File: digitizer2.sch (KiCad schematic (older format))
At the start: 4 parts, among them U1 XC7A35T, U2 FT2232H, U3 MT41J128M16, U4 ADS5403

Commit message: Serial interfaces, cleanup
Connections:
- net ADC_RESET is gone; now on net ADC_SRESET: U4.B12 (SRESET)
- net ADC_SCLK: now also U1.P1 (IO_L4N_T0_34)
- net ADC_SDENB: now also U1.R1 (IO_L7N_T1_34)
- net ADC_SDIO: now also U1.N1 (IO_L4P_T0_34)
- net ADC_SRESET: now reaches U1.N2 (IO_L3N_T0_DQS_34)
- net ADC_SDO: no longer names the net of U4.A10 (SDO)
- no-connect marks 19 -> 20
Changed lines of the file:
@@
 Text Label 13350 9550 0    60   ~ 0
 ADC_SDIO
-Text Label 13350 9650 0    60   ~ 0
-ADC_SDO
 Text Label 13350 9750 0    60   ~ 0
 ADC_SDENB
@@
 USB_CLKOUT
 Text Label 13350 9250 0    60   ~ 0
-ADC_RESET
+ADC_SRESET
+NoConn ~ 13350 9650
+Text Label 9250 1600 0    60   ~ 0
+ADC_SDIO
+Text Label 9250 1500 0    60   ~ 0
+ADC_SRESET
+Text Label 9250 1700 0    60   ~ 0
+ADC_SCLK
+Text Label 9250 2300 0    60   ~ 0
+ADC_SDENB
 $EndSCHEMATC

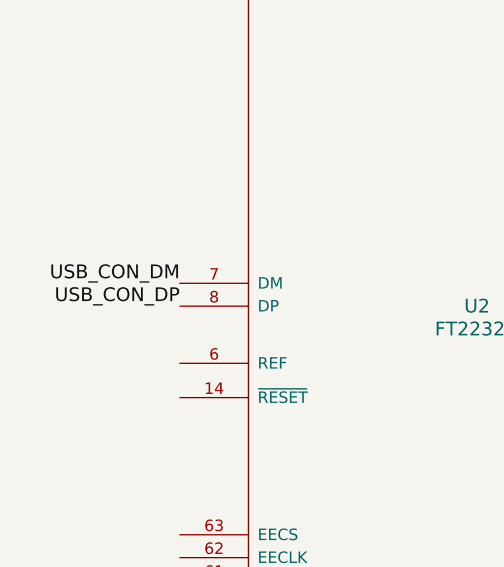
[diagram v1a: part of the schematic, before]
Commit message: Add ADC evaluation board documents, add usb tracks
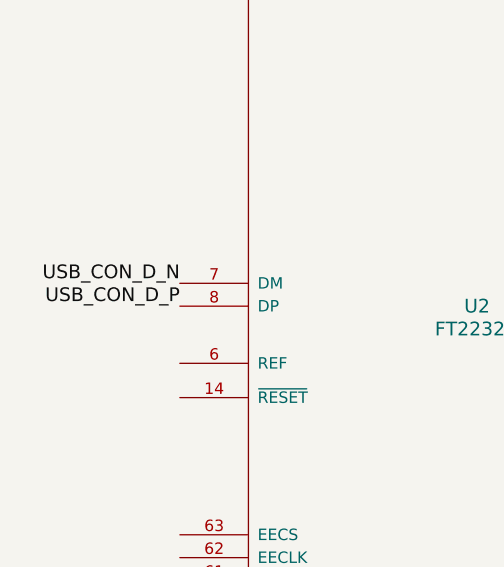
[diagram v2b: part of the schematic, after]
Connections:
- net USB_CON_DM renamed USB_CON_D_N
- net USB_CON_DP renamed USB_CON_D_P
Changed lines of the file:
@@
 Connection ~ 1650 13250
 Text Label 750  10900 2    60   ~ 0
-USB_CON_DM
+USB_CON_D_N
 Text Label 750  11000 2    60   ~ 0
-USB_CON_DP
+USB_CON_D_P
 Text Label 9650 10250 2    60   ~ 0
 ADC_INA_P

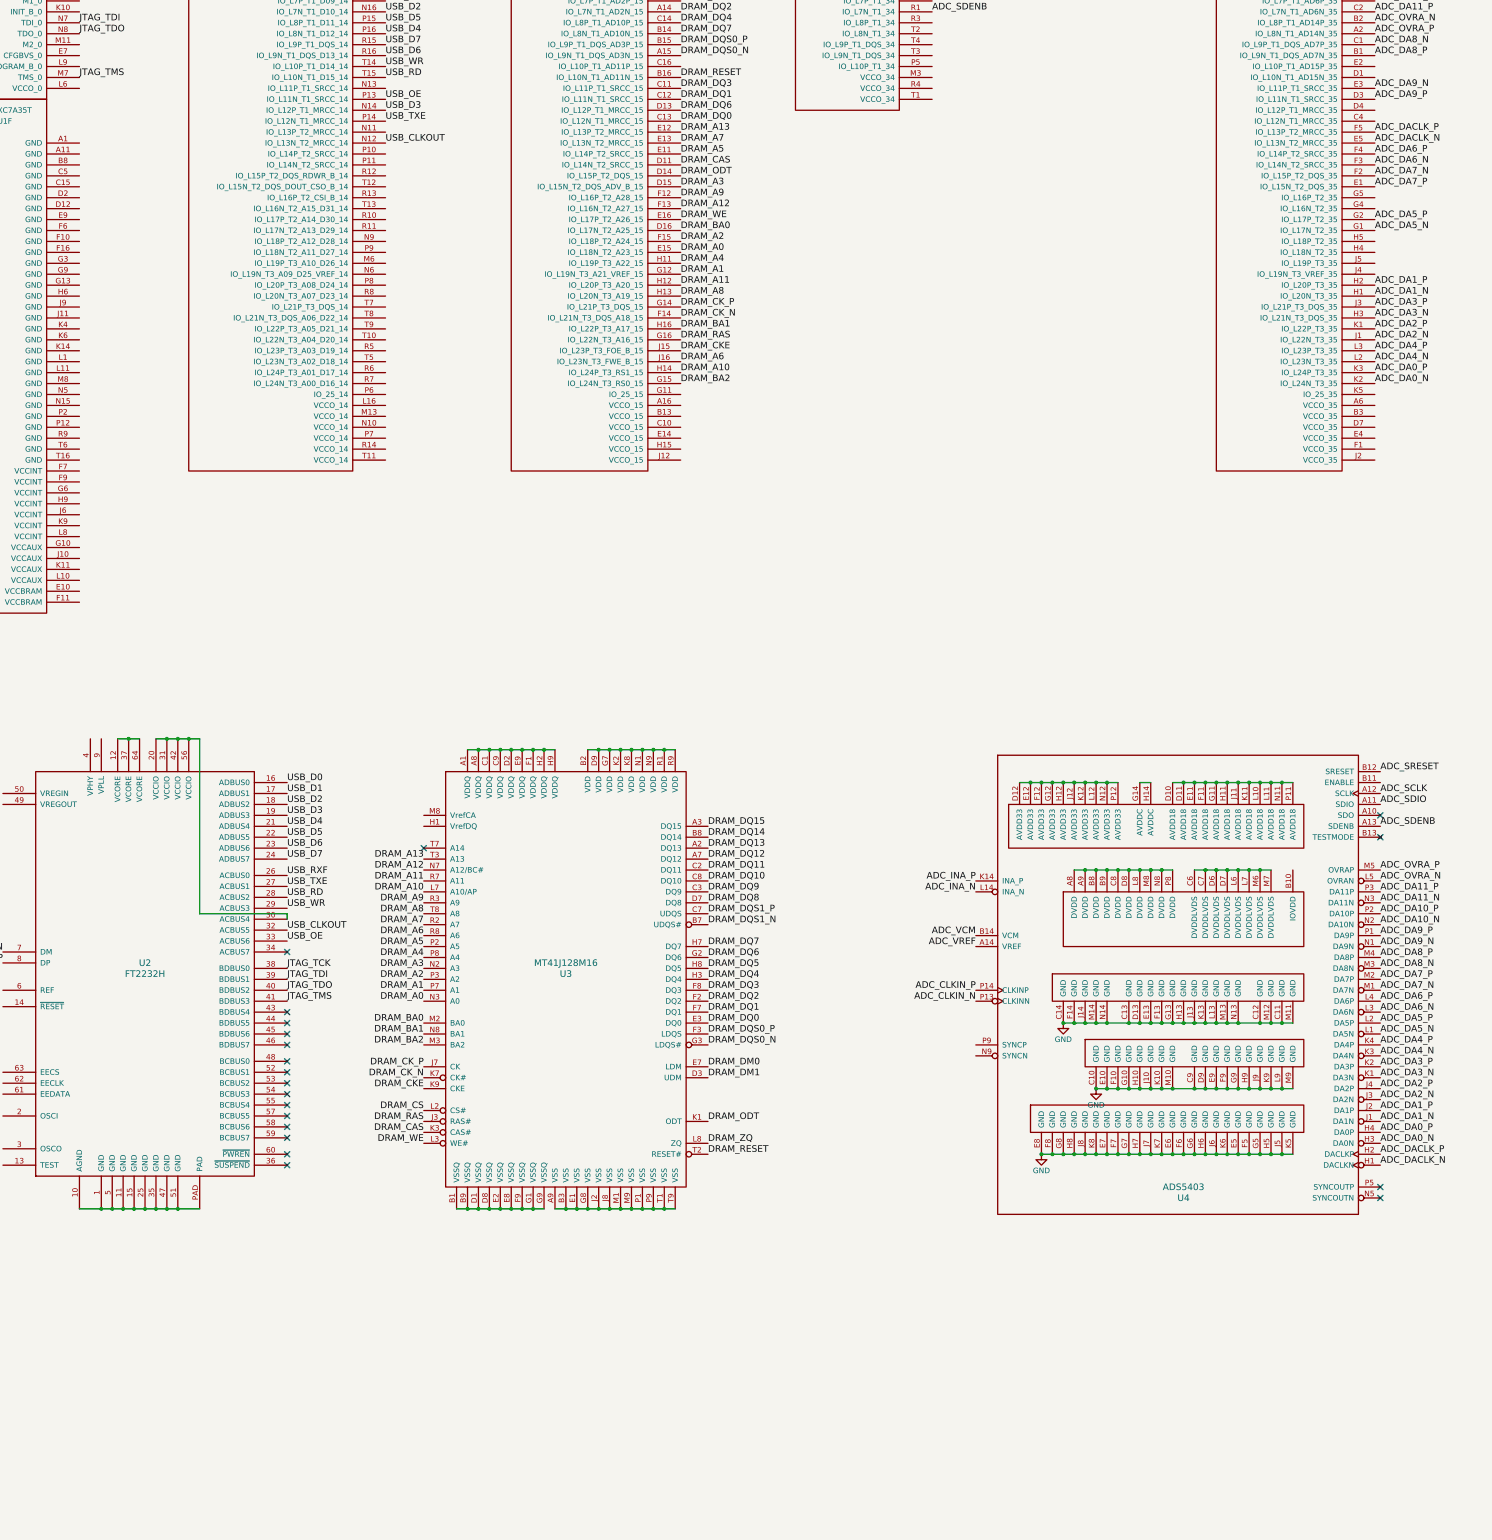
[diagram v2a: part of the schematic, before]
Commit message: Power supply initial selection
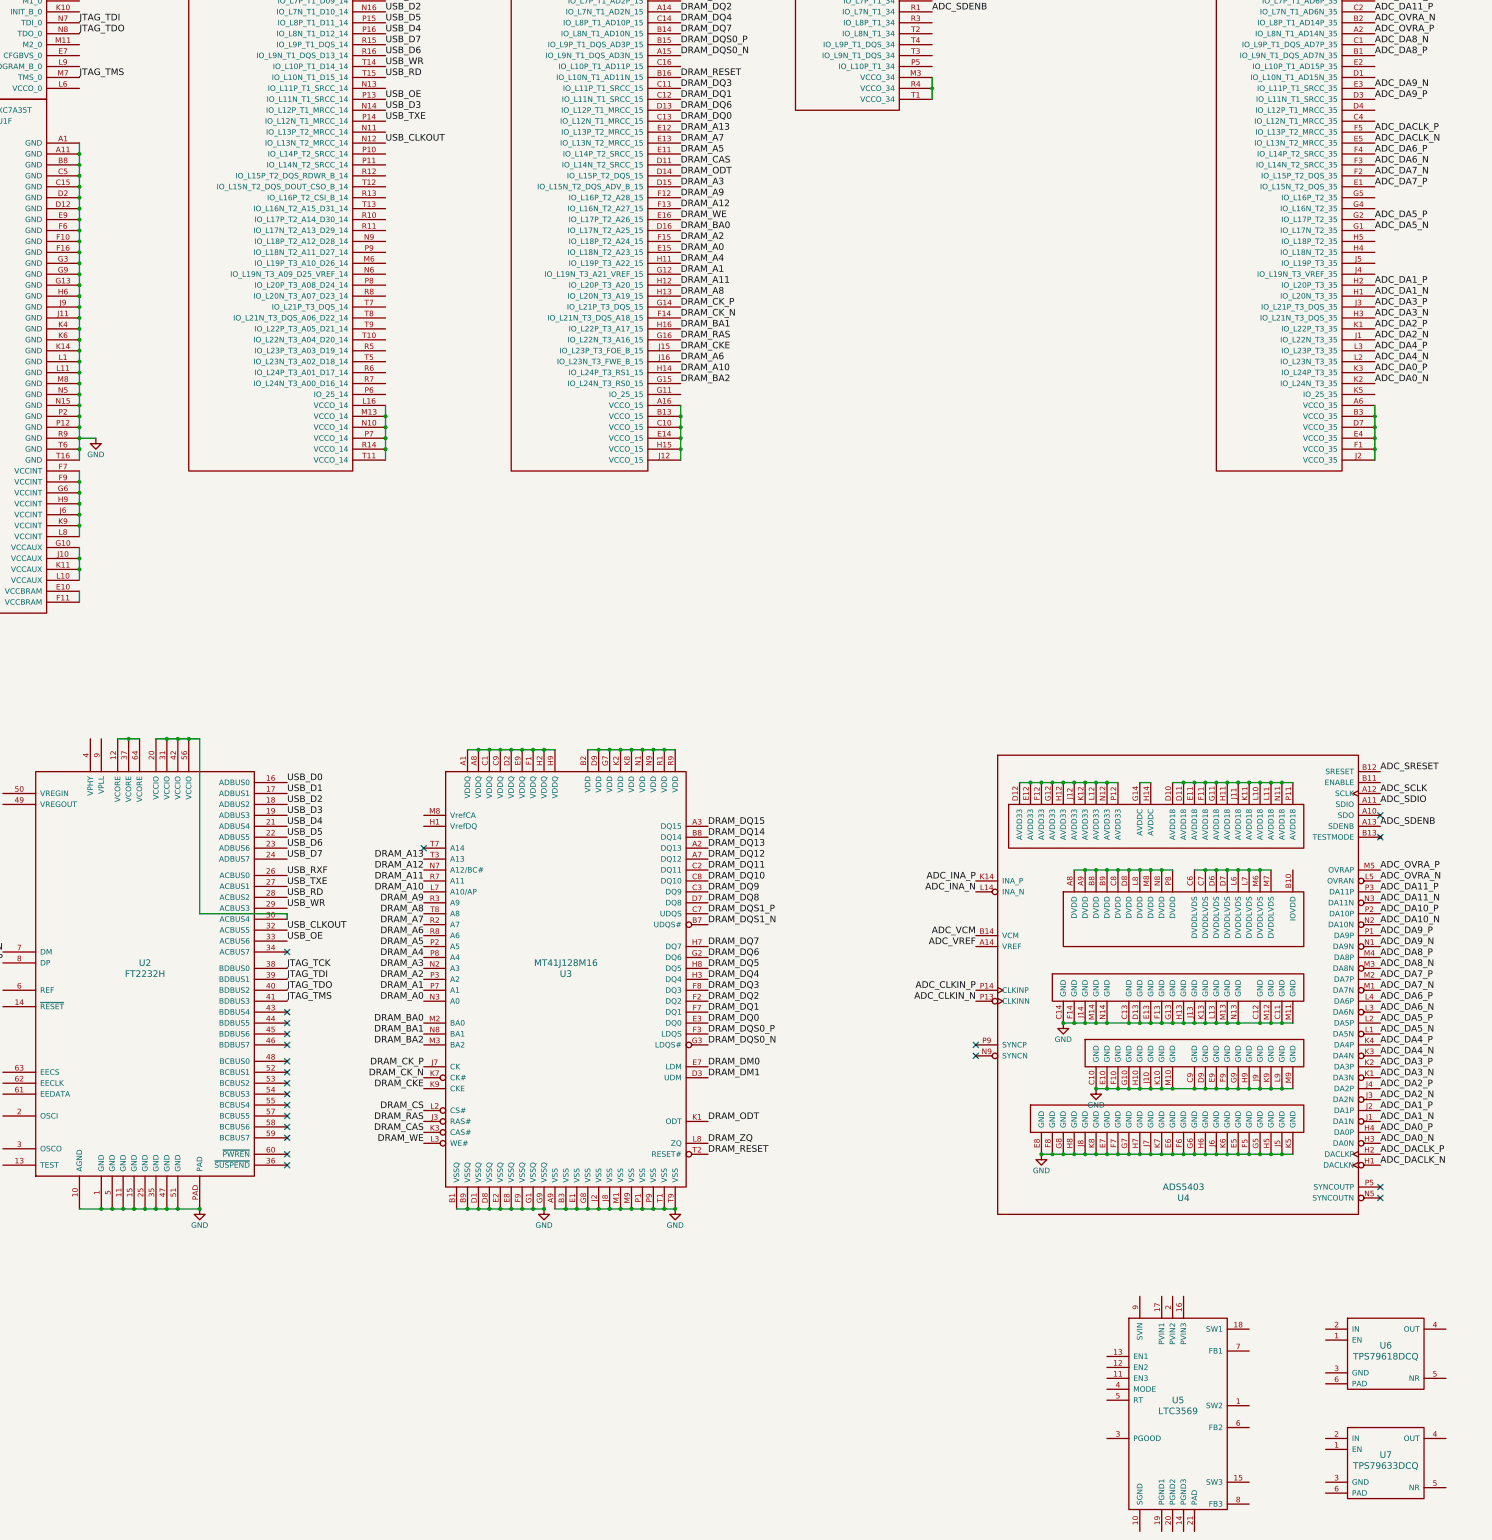
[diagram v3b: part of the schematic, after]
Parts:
- added U5: LTC3569, Housings_DFN_QFN:UQFN-20-1EP_3x3mm_Pitch0.4mm, symbol LTC3569
- added U6: TPS79618DCQ, digitizer2_modules:SOT-223-6, symbol TPS79618DCQ
- added U7: TPS79633DCQ, digitizer2_modules:SOT-223-6, symbol TPS79633DCQ
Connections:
- net GND: now also U1.A1 (GND), U1.A11 (GND), U1.B8 (GND), U1.C15 (GND), U1.C5 (GND), U1.D12 (GND), U1.D2 (GND), U1.E9 (GND), U1.F10 (GND), U1.F16 (GND), U1.F6 (GND), U1.G13 (GND), U1.G3 (GND), U1.G9 (GND), U1.H6 (GND), U1.J11 (GND), U1.J9 (GND), U1.K14 (GND), U1.K4 (GND), U1.K6 (GND), U1.L1 (GND), U1.L11 (GND), U1.M8 (GND), U1.N15 (GND), U1.N5 (GND), U1.P12 (GND), U1.P2 (GND), U1.R9 (GND), U1.T16 (GND), U1.T6 (GND), U2.1 (GND), U2.10 (AGND), U2.11 (GND), U2.15 (GND), U2.25 (GND), U2.35 (GND), U2.47 (GND), U2.5 (GND), U2.51 (GND), U2.PAD, U3.A9 (VSS), U3.B1 (VSSQ), U3.B3 (VSS), U3.B9 (VSSQ), U3.D1 (VSSQ), U3.D8 (VSSQ), U3.E1 (VSS), U3.E2 (VSSQ), U3.E8 (VSSQ), U3.F9 (VSSQ), U3.G1 (VSSQ), U3.G8 (VSS), U3.G9 (VSSQ), U3.J2 (VSS), U3.J8 (VSS), U3.M1 (VSS), U3.M9 (VSS), U3.P1 (VSS), U3.P9 (VSS), U3.T1 (VSS), U3.T9 (VSS)
- net at U1.L16 (VCCO_14): now also U1.M13 (VCCO_14), U1.N10 (VCCO_14), U1.P7 (VCCO_14), U1.R14 (VCCO_14), U1.T11 (VCCO_14)
- net at U1.A16 (VCCO_15): now also U1.B13 (VCCO_15), U1.C10 (VCCO_15), U1.E14 (VCCO_15), U1.H15 (VCCO_15), U1.J12 (VCCO_15)
- net at U1.M3 (VCCO_34): now also U1.R4 (VCCO_34), U1.T1 (VCCO_34)
- net at U1.A6 (VCCO_35): now also U1.B3 (VCCO_35), U1.D7 (VCCO_35), U1.E4 (VCCO_35), U1.F1 (VCCO_35), U1.J2 (VCCO_35)
- net at U1.E10 (VCCBRAM): now also U1.F11 (VCCBRAM)
- net at U1.F7 (VCCINT): now also U1.F9 (VCCINT), U1.G6 (VCCINT), U1.H9 (VCCINT), U1.J6 (VCCINT), U1.K9 (VCCINT), U1.L8 (VCCINT)
- net at U1.G10 (VCCAUX): now also U1.J10 (VCCAUX), U1.K11 (VCCAUX), U1.L10 (VCCAUX)
- no-connect marks 20 -> 22
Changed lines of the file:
@@
 $EndComp
 $Comp
-L GND #PWR01
+L GND #PWR6
 U 1 1 56D761B1
 P 10450 11550
-F 0 "#PWR01" H 10450 11300 50  0001 C CNN
+F 0 "#PWR6" H 10450 11300 50  0001 C CNN
 F 1 "GND" H 10450 11400 50  0000 C CNN
 F 2 "" H 10450 11550 50  0000 C CNN
@@
 $EndComp
 $Comp
-L GND #PWR02
+L GND #PWR7
 U 1 1 56D76204
 P 10750 12150
-F 0 "#PWR02" H 10750 11900 50  0001 C CNN
+F 0 "#PWR7" H 10750 11900 50  0001 C CNN
 F 1 "GND" H 10750 12000 50  0000 C CNN
 F 2 "" H 10750 12150 50  0000 C CNN
@@
 $EndComp
 $Comp
-L GND #PWR03
+L GND #PWR5
 U 1 1 56D764BB
 P 10250 12750
-F 0 "#PWR03" H 10250 12500 50  0001 C CNN
+F 0 "#PWR5" H 10250 12500 50  0001 C CNN
 F 1 "GND" H 10250 12600 50  0000 C CNN
 F 2 "" H 10250 12750 50  0000 C CNN
@@
 Text Label 9250 2300 0    60   ~ 0
 ADC_SDENB
+Wire Wire Line
+	1450 3500 1450 6400
+Connection ~ 1450 3600
+Connection ~ 1450 3700
+Connection ~ 1450 3800
+Connection ~ 1450 3900
+Connection ~ 1450 4000
+Connection ~ 1450 4100
+Connection ~ 1450 4200
+Connection ~ 1450 4300
+Connection ~ 1450 4400
+Connection ~ 1450 4500
+Connection ~ 1450 4600
+Connection ~ 1450 4700
+Connection ~ 1450 4800
+Connection ~ 1450 4900
+Connection ~ 1450 5000
+Connection ~ 1450 5100
+Connection ~ 1450 5200
+Connection ~ 1450 5300
+Connection ~ 1450 5400
+Connection ~ 1450 5500
+Connection ~ 1450 5600
+Connection ~ 1450 5700
+Connection ~ 1450 5800
+Connection ~ 1450 5900
+Connection ~ 1450 6000
+Connection ~ 1450 6100
+Connection ~ 1450 6200
+Connection ~ 1450 6300
+Wire Wire Line
+	1450 6500 1450 7100
+Wire Wire Line
+	1450 7200 1450 7500
+Wire Wire Line
+	1450 7600 1450 7700
+Connection ~ 1450 7300
+Connection ~ 1450 7400
+Connection ~ 1450 6600
+Connection ~ 1450 6700
+Connection ~ 1450 6800
+Connection ~ 1450 6900
+Connection ~ 1450 7000
+Wire Wire Line
+	6950 5900 6950 6400
+Connection ~ 6950 6000
+Connection ~ 6950 6100
+Connection ~ 6950 6200
+Connection ~ 6950 6300
+Wire Wire Line
+	9250 2900 9250 3100
+Connection ~ 9250 3000
+Wire Wire Line
+	13300 5900 13300 6400
+Connection ~ 13300 6000
+Connection ~ 13300 6100
+Connection ~ 13300 6200
+Connection ~ 13300 6300
+Wire Wire Line
+	4250 5900 4250 6400
+Connection ~ 4250 6000
+Connection ~ 4250 6100
+Connection ~ 4250 6200
+Connection ~ 4250 6300
+$Comp
+L GND #PWR2
+U 1 1 56EA5E1A
+P 2550 13250
+F 0 "#PWR2" H 2550 13000 50  0001 C CNN
+F 1 "GND" H 2550 13100 50  0000 C CNN
+F 2 "" H 2550 13250 50  0000 C CNN
+F 3 "" H 2550 13250 50  0000 C CNN
+	1    2550 13250
+	1    0    0    -1
+$EndComp
+Connection ~ 2550 13250
+$Comp
+L GND #PWR3
+U 1 1 56EA60EC
+P 5700 13250
+F 0 "#PWR3" H 5700 13000 50  0001 C CNN
+F 1 "GND" H 5700 13100 50  0000 C CNN
+F 2 "" H 5700 13250 50  0000 C CNN
+F 3 "" H 5700 13250 50  0000 C CNN
+	1    5700 13250
+	1    0    0    -1
+$EndComp
+$Comp
+L GND #PWR4
+U 1 1 56EA6136
+P 6900 13250
+F 0 "#PWR4" H 6900 13000 50  0001 C CNN
+F 1 "GND" H 6900 13100 50  0000 C CNN
+F 2 "" H 6900 13250 50  0000 C CNN
+F 3 "" H 6900 13250 50  0000 C CNN
+	1    6900 13250
+	1    0    0    -1
+$EndComp
+Connection ~ 6900 13250
+Connection ~ 5700 13250
+$Comp
+L GND #PWR1
+U 1 1 56EA687A
+P 1600 6200
+F 0 "#PWR1" H 1600 5950 50  0001 C CNN
+F 1 "GND" H 1600 6050 50  0000 C CNN
+F 2 "" H 1600 6200 50  0000 C CNN
+F 3 "" H 1600 6200 50  0000 C CNN
+	1    1600 6200
+	1    0    0    -1
+$EndComp
+Wire Wire Line
+	1600 6200 1450 6200
+NoConn ~ 9650 11750
+NoConn ~ 9650 11850
+$Comp
+L LTC3569 U5
+U 1 1 56EAC1FD
+P 11500 15050
+F 0 "U5" H 11500 15100 60  0000 C CNN
+F 1 "LTC3569" H 11500 15000 60  0000 C CNN
+F 2 "Housings_DFN_QFN:UQFN-20-1EP_3x3mm_Pitch0.4mm" H 11500 15100 60  0001 C CNN
+F 3 "" H 11500 15100 60  0000 C CNN
+	1    11500 15050
+	1    0    0    -1
+$EndComp
+$Comp
+L TPS79618DCQ U6
+U 1 1 56EAE74F
+P 13400 14600
+F 0 "U6" H 13400 14700 60  0000 C CNN
+F 1 "TPS79618DCQ" H 13400 14600 60  0000 C CNN
+F 2 "digitizer2_modules:SOT-223-6" H 13400 14600 60  0001 C CNN
+F 3 "" H 13400 14600 60  0000 C CNN
+	1    13400 14600
+	1    0    0    -1
+$EndComp
+$Comp
+L TPS79633DCQ U7
+U 1 1 56EAEBFC
+P 13400 15600
+F 0 "U7" H 13400 15700 60  0000 C CNN
+F 1 "TPS79633DCQ" H 13400 15600 60  0000 C CNN
+F 2 "digitizer2_modules:SOT-223-6" H 13400 15600 60  0001 C CNN
+F 3 "" H 13400 15600 60  0000 C CNN
+	1    13400 15600
+	1    0    0    -1
+$EndComp
 $EndSCHEMATC

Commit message: Config bank. Power labels
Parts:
- added R1, R2: 4.7k, symbol R
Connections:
- net DRAM_CS is gone; now on net GND: U3.L2 (CS#)
- net DRAM_DM0 is gone; now on net GND: U3.E7 (LDM)
- net DRAM_DM1 is gone; now on net GND: U3.D3 (UDM)
- net GND: now also U1.G7 (GNDADC_0), U1.H7 (VREFN_0), U1.J8 (VREFP_0), U1.K7 (DXN_0), U1.K8 (DXP_0), U1.L15 (IO_L3P_T0_DQS_PUDC_B_14), U1.M10 (M1_0), U2.13 (TEST)
- net VDD_FPGA_3V3: now reaches U1.E7 (CFGBVS_0)
- net VDD_FPGA_3V3: now also U1.L16 (VCCO_14), U1.L6 (VCCO_0), U1.M11 (M2_0), U1.M13 (VCCO_14), U1.M9 (M0_0), U1.N10 (VCCO_14), U1.P7 (VCCO_14), U1.R14 (VCCO_14), U1.T11 (VCCO_14), U2.20 (VCCIO), U2.30 (ACBUS4), U2.31 (VCCIO), U2.42 (VCCIO), U2.50 (VREGIN), U2.56 (VCCIO), R1.1, R2.1
- net VDD_FPGA_1V8: now reaches U1.F8 (VCCBATT_0)
- net VDD_FPGA_1V8: now also U1.G10 (VCCAUX), U1.G8 (VCCADC_0), U1.J10 (VCCAUX), U1.K11 (VCCAUX), U1.L10 (VCCAUX)
- net INIT_B: now reaches U1.K10 (INIT_B_0)
- net INIT_B: now also R2.2
- net PROGRAM_B: now reaches U1.L9 (PROGRAM_B_0)
- net PROGRAM_B: now also R1.2
- net VDD_DRAM_1V5: now reaches U1.A16 (VCCO_15), U1.B13 (VCCO_15), U1.C10 (VCCO_15), U1.E14 (VCCO_15), U1.H15 (VCCO_15), U1.J12 (VCCO_15)
- net VDD_DRAM_1V5: now also U3.A1 (VDDQ), U3.A8 (VDDQ), U3.B2 (VDD), U3.C1 (VDDQ), U3.C9 (VDDQ), U3.D2 (VDDQ), U3.D9 (VDD), U3.E9 (VDDQ), U3.F1 (VDDQ), U3.G7 (VDD), U3.H2 (VDDQ), U3.H9 (VDDQ), U3.K2 (VDD), U3.K8 (VDD), U3.N1 (VDD), U3.N9 (VDD), U3.R1 (VDD), U3.R9 (VDD)
- net VDD_ADC_1V8: now reaches U1.A6 (VCCO_35), U1.B3 (VCCO_35), U1.D7 (VCCO_35), U1.E4 (VCCO_35), U1.F1 (VCCO_35), U1.J2 (VCCO_35)
- net VDD_ADC_1V8: now also U4.A8 (DVDD), U4.A9 (DVDD), U4.B8 (DVDD), U4.B9 (DVDD), U4.C6 (DVDDLVDS), U4.C7 (DVDDLVDS), U4.C8 (DVDD), U4.D10 (AVDD18), U4.D11 (AVDD18), U4.D6 (DVDDLVDS), U4.D7 (DVDDLVDS), U4.D8 (DVDD), U4.E11 (AVDD18), U4.F11 (AVDD18), U4.G11 (AVDD18), U4.G14 (AVDDC), U4.H11 (AVDD18), U4.H14 (AVDDC), U4.J11 (AVDD18), U4.K11 (AVDD18), U4.L10 (AVDD18), U4.L11 (AVDD18), U4.L6 (DVDDLVDS), U4.L7 (DVDDLVDS), U4.L8 (DVDD), U4.M6 (DVDDLVDS), U4.M7 (DVDDLVDS), U4.M8 (DVDD), U4.N11 (AVDD18), U4.N8 (DVDD), U4.P11 (AVDD18), U4.P8 (DVDD)
- net VDD_FPGA_1V0: now reaches U1.E10 (VCCBRAM), U1.F11 (VCCBRAM)
- net VDD_FPGA_1V0: now also U1.F7 (VCCINT), U1.F9 (VCCINT), U1.G6 (VCCINT), U1.H9 (VCCINT), U1.J6 (VCCINT), U1.K9 (VCCINT), U1.L8 (VCCINT)
- net VDD_FTDI_1V8: now reaches U2.12 (VCORE), U2.37 (VCORE), U2.64 (VCORE)
- net VDD_FTDI_1V8: now also U2.49 (VREGOUT)
- net VDD_ADC_3V3: now reaches U4.D12 (AVDD33), U4.E12 (AVDD33), U4.F12 (AVDD33), U4.G12 (AVDD33), U4.H12 (AVDD33), U4.J12 (AVDD33), U4.K12 (AVDD33), U4.L12 (AVDD33), U4.N12 (AVDD33), U4.P12 (AVDD33)
- no-connect marks 22 -> 26
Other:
- moved on the sheet: U3, U4, U5, U6, U7

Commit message: Cleanup. Add Eeprom.
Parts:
- added U8: 93LC46BT-I/OT, digitizer2_modules:SOT-23-6, symbol 93LC46BT-I/OT
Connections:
- no-connect marks 26 -> 27
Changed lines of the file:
@@
 GND
 NoConn ~ 1450 900
+NoConn ~ 3750 19950
+$Comp
+L 93LC46BT-I/OT U8
+U 1 1 56EF2009
+P -250 12200
+F 0 "U8" H -400 12550 50  0000 C CNN
+F 1 "93LC46BT-I/OT" H -450 11950 50  0000 L CNN
+F 2 "digitizer2_modules:SOT-23-6" H -350 12200 50  0001 C CNN
+F 3 "" H -250 12300 50  0000 C CNN
+	1    -250 12200
+	1    0    0    -1
+$EndComp
 $EndSCHEMATC
